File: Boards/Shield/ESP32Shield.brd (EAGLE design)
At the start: 160 x 75.9 mm, 28 parts, among them Q1 220mA/50V/3.5Ω, U1 5V

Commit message: began layout
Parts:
- added J4: (no value), SparkFun-Connectors:1X01
- LEFTEYE, RIGHTEYE: device SparkFun-Connectors:1X04_1MM_RA -> SparkFun-Connectors:1X04
- moved J3 142.6 mm to (57.1, 1.27)
- moved J2 136.9 mm to (57.1, 6.35)
- moved C2 109.7 mm to (33.0, 40.6)
- moved J1 104.2 mm to (36.8, 20.3), turned to 270 degrees
- moved LEFTEYE 103.1 mm to (14.0, -3.81)
- moved S3 102.9 mm to (49.5, 22.9)
- moved C3 100.1 mm to (36.8, 11.4), turned to 90 degrees
- moved R31 99.7 mm to (52.1, 16.5)
- moved R4 93.4 mm to (38.1, 5.08), turned to 90 degrees
- moved F3 89.9 mm to (10.2, 12.7), turned to 90 degrees
- moved U1 89.1 mm to (10.2, 7.62), turned to 180 degrees
- moved R3 89.1 mm to (35.6, 5.08), turned to 90 degrees
- moved S1 87.5 mm to (63.5, 22.9)
- moved R36 84.5 mm to (36.8, 26.7), turned to 180 degrees
- moved RIGHTEYE 74.5 mm to (1.27, -3.81)
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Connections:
- removed net 5VR: C2.1, C3.+, R1.2, U$2.4, U$2.5
- removed net POWER: Q1.1
- net 5V: now also C2.1, C3.+, J4.1, R1.2, U$2.4, U$2.5
- net GND: now also Q1.1
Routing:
- added copper zone on layer 1, net GND
- added copper zone on layer 16, net GND
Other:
- board size 160 x 75.9 mm -> 160 x 81 mm
- board text added: "C"
- board text added: "D"
- board text added: "G"
- board text added: "V"

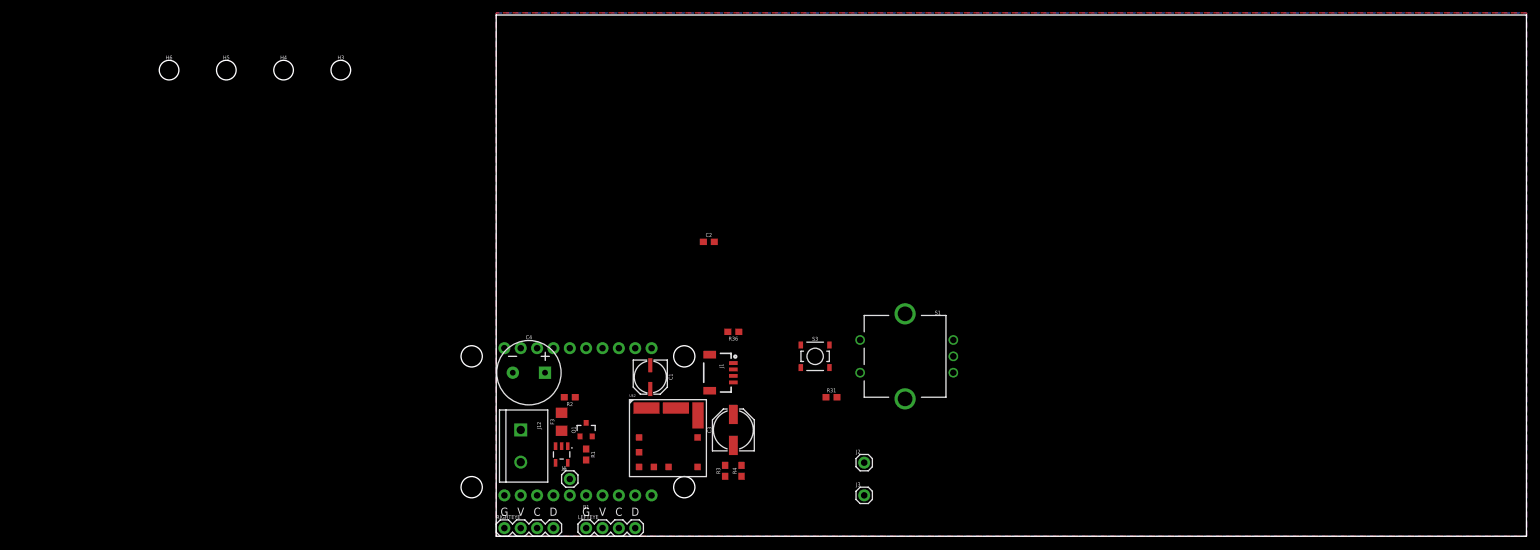
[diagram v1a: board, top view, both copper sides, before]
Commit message: finished ESP32 Shield layout
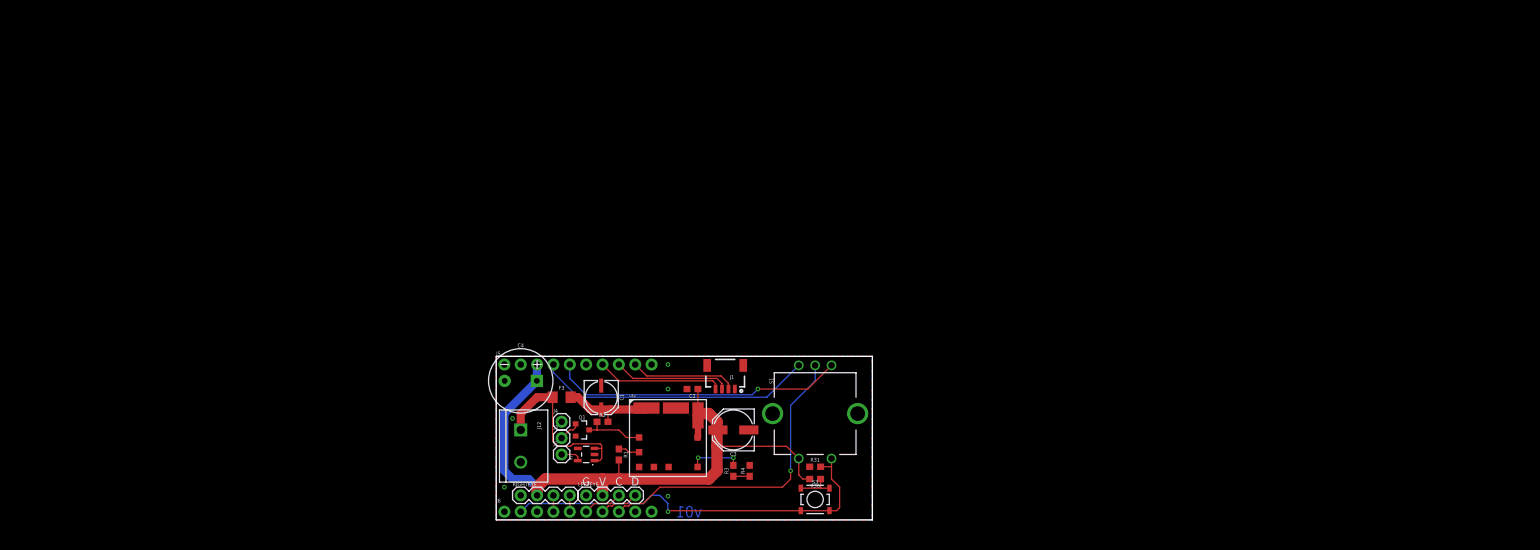
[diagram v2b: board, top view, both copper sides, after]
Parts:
- removed B1: SPARKFUN_ESP8266_THING_DEV, SparkFun-Boards:SPARKFUN_ESP8266_THING_DEV
- removed H3, H4, H5, H6: STAND-OFFTIGHT, SparkFun-Hardware:STAND-OFF-TIGHT
- added J5, J6: (no value), SparkFun-Connectors:1X10_NO_SILK
- moved FRAME1 114.4 mm to (-2.54, -10.2)
- moved J3 47.8 mm to (10.2, 10.2)
- moved J2 47.0 mm to (10.2, 7.62)
- moved R36 26.2 mm to (49.5, 3.81)
- moved C2 23.0 mm to (30.5, 17.8), turned to 180 degrees
- moved S3 22.2 mm to (49.5, 0.64)
- moved S1 16.6 mm to (49.5, 14.0), turned to 90 degrees
- moved R31 11.1 mm to (49.5, 5.71)
- moved J4 8.98 mm to (10.2, 12.7)
- moved C1 8.25 mm to (16.5, 16.5)
- moved R2 6.35 mm to (16.5, 12.7), turned to 0 degrees
- moved RIGHTEYE 5.68 mm to (3.81, 1.27)
- moved LEFTEYE 5.08 mm to (14.0, 1.27)
- moved R1 5.08 mm to (19.1, 7.62)
- moved F3 3.81 mm to (10.2, 16.5), turned to 0 degrees
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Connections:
- removed net VIN: B1.VIN
- new net N$1: J3.1, Q1.1
- net 3.3V: now also J5.9; no longer B1.3.3V
- net 5V: now also J5.3; no longer B1.5V, J4.1
- net BTN: now also J6.2; no longer B1.ADC
- net CL: now also J6.6; no longer B1.4
- net CR: now also J6.4; no longer B1.12
- net DL: now also J6.7; no longer B1.0
- net DR: now also J6.5; no longer B1.13
- net ENC-A: now also J5.5; no longer B1.TX
- net ENC-B: now also J5.4; no longer B1.RX
- net ENC-C: now also J6.8; no longer B1.5
- net GND: now also J4.1, J5.1, J5.10, J6.10; no longer B1.GND@1, B1.GND@2, B1.GND@3, J3.1, Q1.1
- net SCL: now also J5.7; no longer B1.14
- net SDA: now also J5.8; no longer B1.2
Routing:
- net 5V: track 0.00 -> 98.7 mm
- net BTN: track 0.00 -> 62.5 mm, vias 0 -> 1
- net ENC-C: track 0.00 -> 48.0 mm, vias 0 -> 1
- net ENC-A: track 0.00 -> 45.7 mm, vias 0 -> 1
- net ENC-B: track 0.00 -> 43.0 mm
- net VBATT: track 0.00 -> 28.0 mm
- net SCL: track 0.00 -> 19.6 mm
- net SDA: track 0.00 -> 18.1 mm
- net 3.3V: track 0.00 -> 16.6 mm
- net N$2: track 0.00 -> 14.7 mm
- net N$3: track 0.00 -> 9.51 mm
- net N$4: track 0.00 -> 8.11 mm, vias 0 -> 2
- net CL: track 0.00 -> 6.13 mm
- net DL: track 0.00 -> 6.13 mm
- net N$17: track 0.00 -> 5.88 mm
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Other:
- board size 160 x 81 mm -> 58.4 x 25.4 mm
- board text added: "Andy England"
- board text added: "REZZ Glasses Control"
- board text added: "v01"
